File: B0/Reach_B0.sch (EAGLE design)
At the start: 237 parts, among them IC1 TMC2130QFN36, IC10 74AHC1G126DCK, IC11 74AHC1G126DCK, IC18 74AHC1G126DCK, IC2 TMC2130QFN36, IC3 74AHC1G126DCK, IC4 74AHC1G126DCK, IC5 74AHC1G126DCK, IC6 74AHC1G126DCK, IC7 74AHC1G126DCK, IC8 TMC2130QFN36, IC9 74AHC1G126DCK, P8 F-2X23-, P9 F-2X23-, Q2 AON6758, Q3 AON6758, U1 SN74AHC595PW, U10 RT8268, U11 PCA9685PW, U18 CAT24C256, U2 SN74AHC595PW, U3 MCP9600, U4 MCP9600, U5 MCP9600, U6 MCP9600, U7 SN74AHC595PW, X1 22-05-7028-02, X11 22-05-7028-02, X14 22-05-7048-04, X2 MSTBA4, X21 MSTBA2, X3 MSTBA2, X4 22-05-7028-02, X5 22-05-7028-02, X6 22-05-7048-04, X7 22-05-7028-02, X8 22-05-7048-04, X9 22-05-7028-02

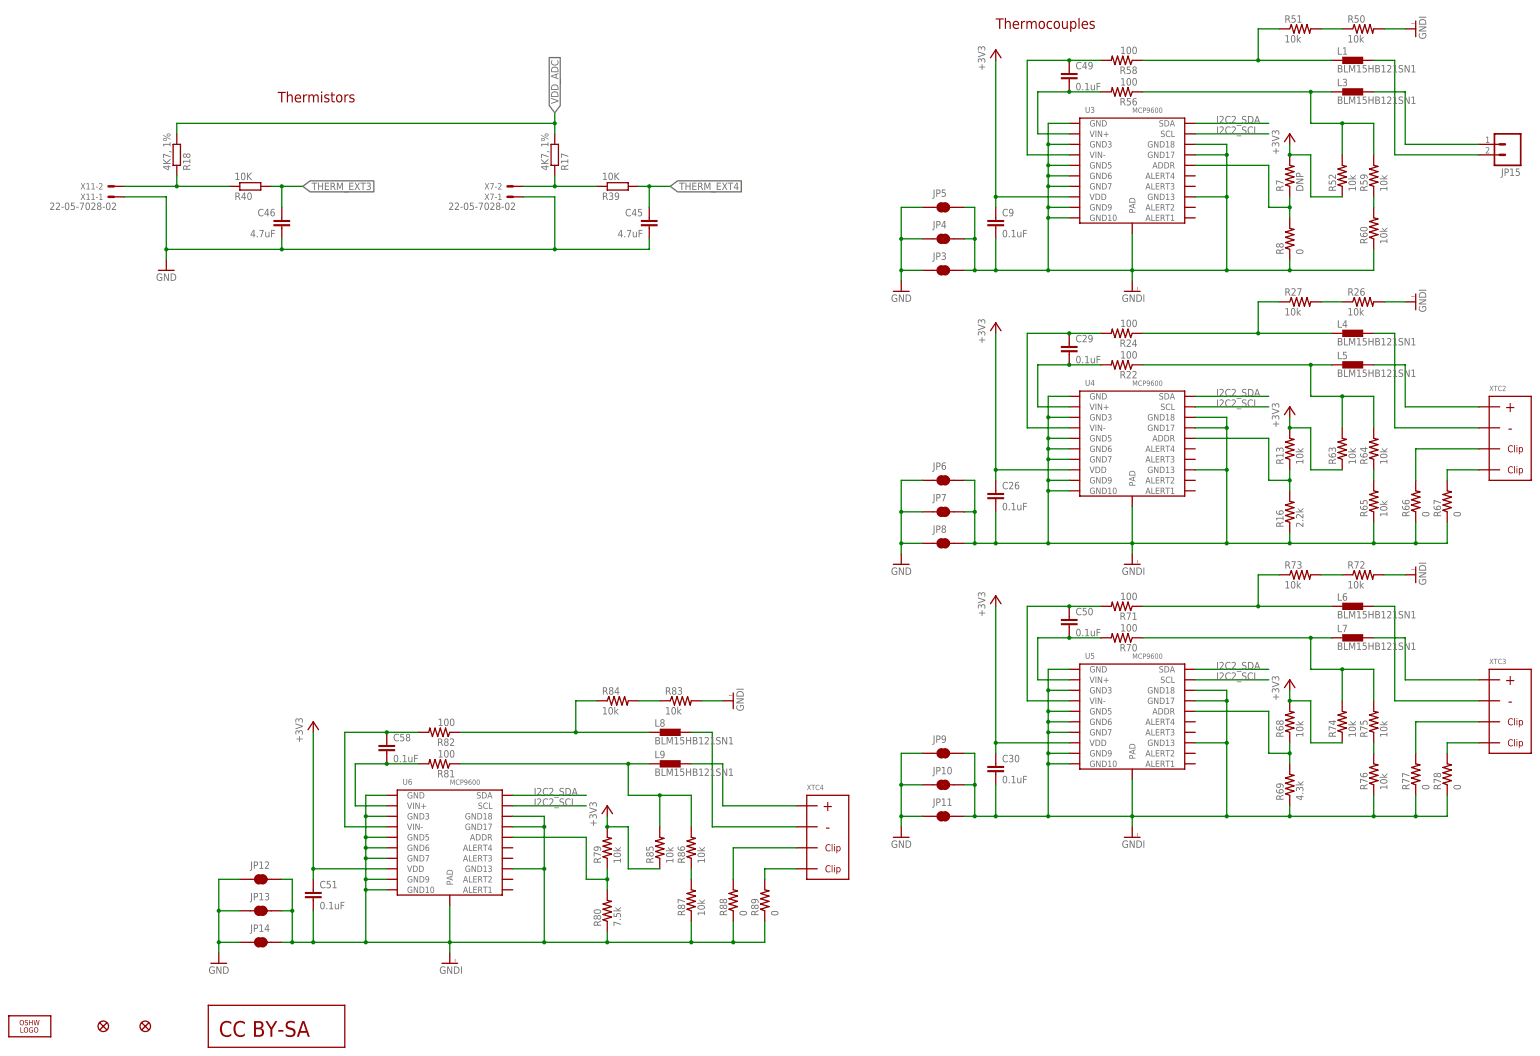
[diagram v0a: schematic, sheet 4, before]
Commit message: removed LCD jumpers
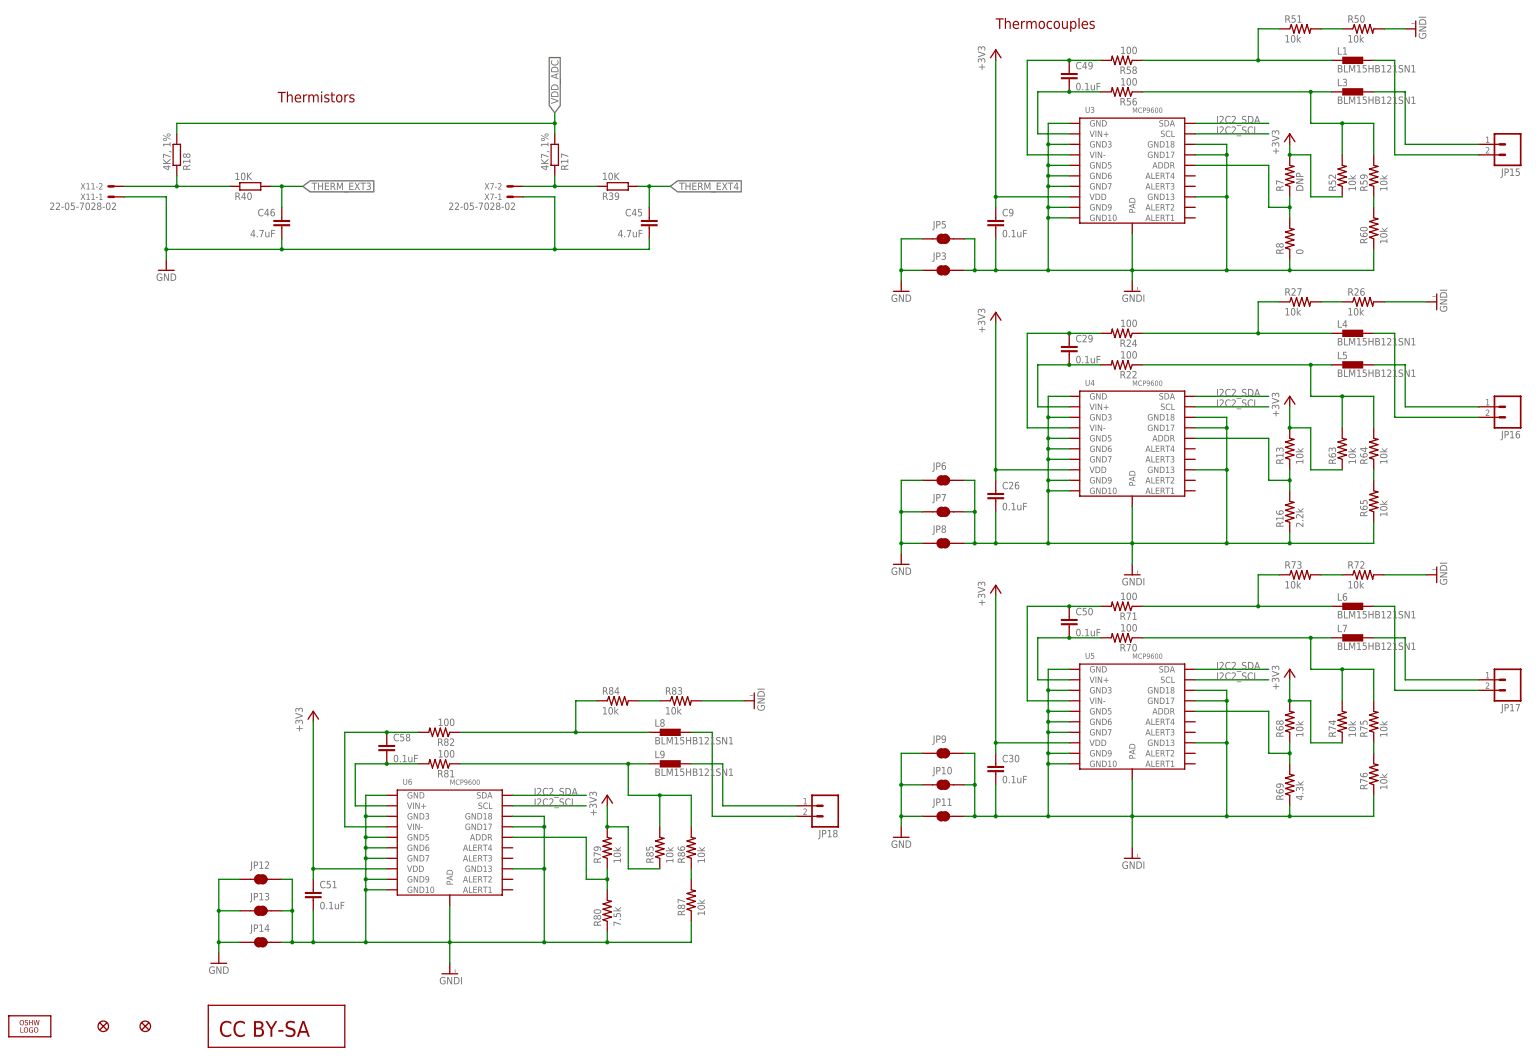
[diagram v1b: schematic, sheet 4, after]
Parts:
- removed JP4: JUMPER-PAD-2-NC_BY_TRACE, SparkFun-PassivesNEW:JUMPER-PAD-2-NC_BY_TRACE
- removed R88, R89: 0, SparkFun-Resistors:RESISTOR0805-RES
- removed XTC2, XTC3, XTC4: NEWPORT_THERMOCOUPLE_CONNECTORPCC-SMP-V, reach_custom:NEWPORT_THERMOCOUPLE_CONNECTORPCC-SMP-V
- added JP16, JP17, JP18: (no value), SparkFun-ConnectorsNEW:M025MM
- added R61, R62: 330, rcl:R-EU_R0402
- JP15: device SparkFun-Connectors:M025MM -> SparkFun-ConnectorsNEW:M025MM
- R66, R67, R77, R78: value 0 -> 330; device SparkFun-Resistors:RESISTOR0805-RES -> rcl:R-EU_R0402
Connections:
- removed net N$134: R88.2, XTC4.P$3
- removed net N$135: R89.2, XTC4.P$4
- removed net N$900: U7.QH_2
- removed net N$97: R77.2, XTC3.P$3
- removed net N$98: R78.2, XTC3.P$4
- new net N$51: Q3.G, R47.2, R61.1
- new net N$73: Q2.G, R48.2, R62.1
- new net N$83: Q1.B, R19.2, R77.1
- new net N$84: Q6.B, R34.2, R78.1
- net FAN4: now also R78.2; no longer Q6.B, R34.2
- net FAN5: now also R77.2; no longer Q1.B, R19.2
- net FAN6: now also R67.2; no longer Q4.B, R21.2
- net FAN7: now also R66.2; no longer Q5.B, R33.2
- net GND: no longer JP4.1
- net GNDI: no longer JP4.2, R66.1, R67.1, R77.1, R78.1, R88.1, R89.1
- net HEATER_A: now also R61.2; no longer Q3.G, R47.2
- net HEATER_B: now also R62.2; no longer Q2.G, R48.2
- net N$123: now also JP18.2; no longer XTC4.P$2
- net N$130: now also JP18.1; no longer XTC4.P$1
- net N$38: now also JP16.2; no longer XTC2.P$2
- net N$47: now also JP16.1; no longer XTC2.P$1
- net N$76: now also Q5.B, R33.2, R66.1; no longer R66.2, XTC2.P$3
- net N$77: now also Q4.B, R21.2, R67.1; no longer R67.2, XTC2.P$4
- net N$87: now also JP17.2; no longer XTC3.P$2
- net N$92: now also JP17.1; no longer XTC3.P$1
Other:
- moved on the sheet: JP5, R19, R21, R33, R34, R47, R48
